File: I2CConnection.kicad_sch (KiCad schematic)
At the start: 15 parts, among them J3 +5V_{IN}, J5 I2C, Q1 Q_NMOS_GSD, Q2 Q_NMOS_GSD

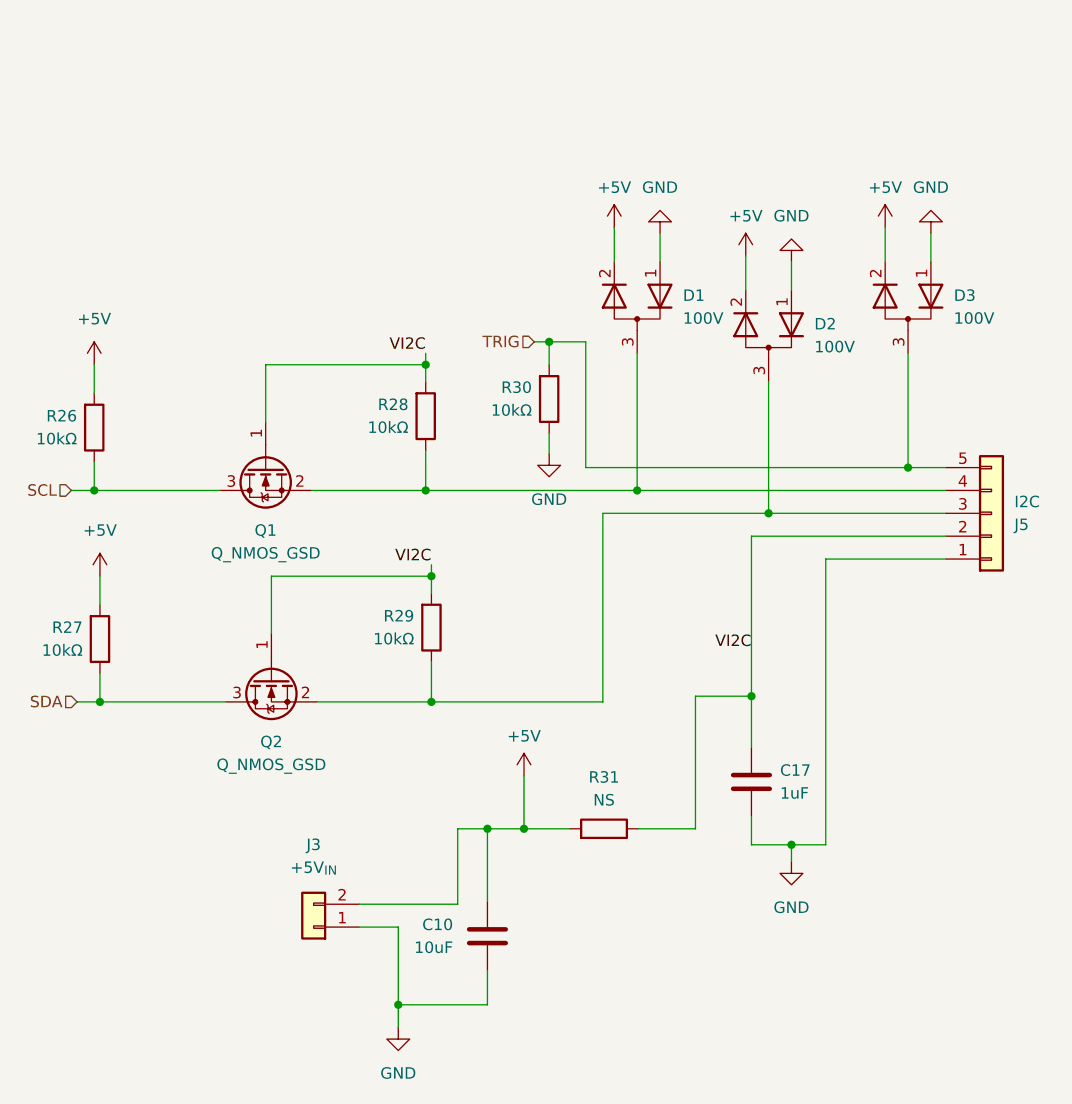
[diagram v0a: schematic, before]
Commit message: Added extra capacitor and reroute the power to better optimize the board.
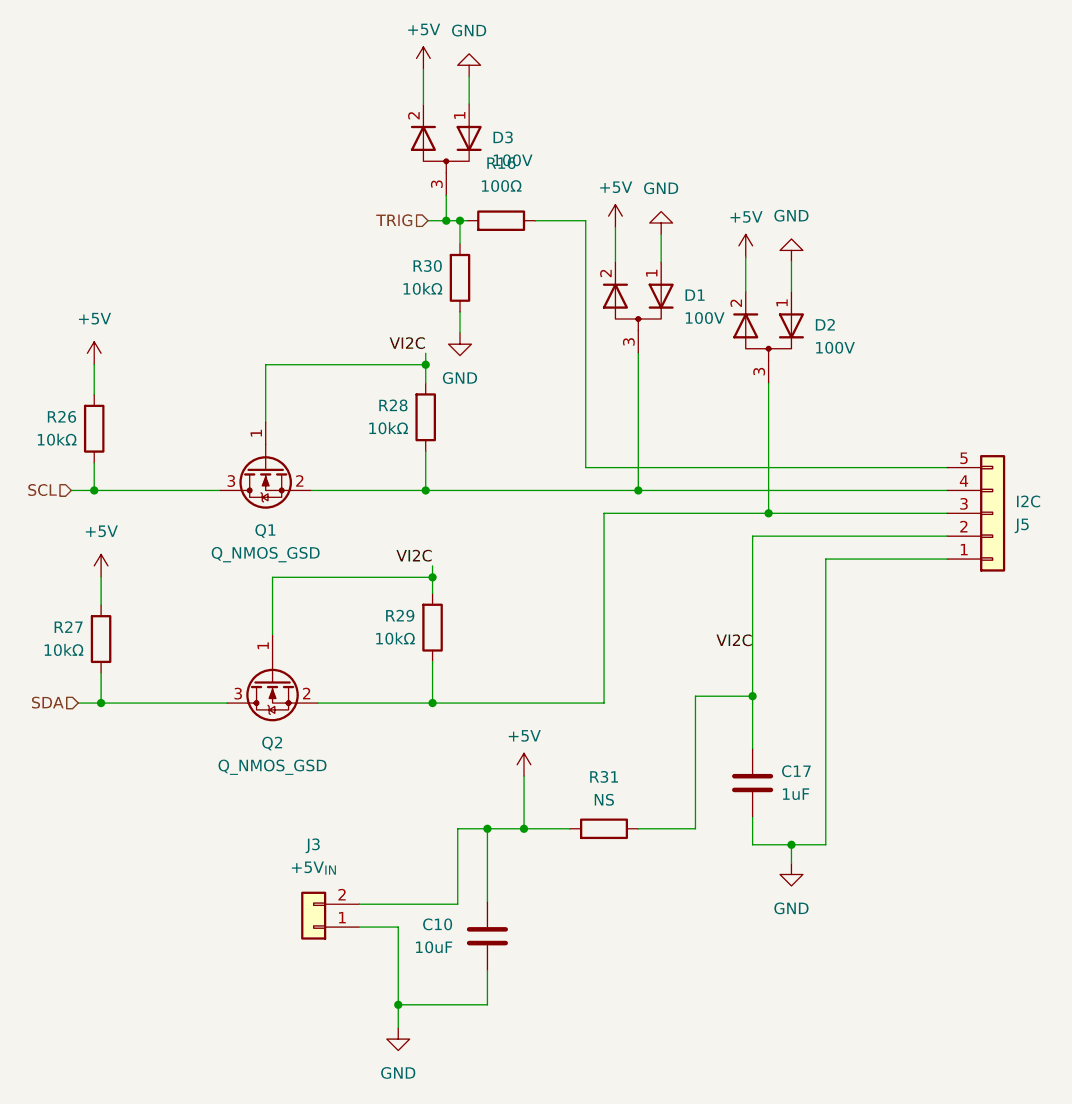
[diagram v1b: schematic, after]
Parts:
- added R16: 100Ω, Resistor_SMD:R_0805_2012Metric, symbol Device:R
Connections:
- net TRIG: now also R16.2; no longer J5.5 (Pin_5)
- new net: J5.5 (Pin_5), R16.1
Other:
- moved on the sheet: D3, R30
